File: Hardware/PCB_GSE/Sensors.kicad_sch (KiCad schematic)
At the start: 18 parts, among them J6 Screw_Terminal_01x04, J7 Screw_Terminal_01x04, U1 MAX6612MXK, U4 INA125UA/2K5

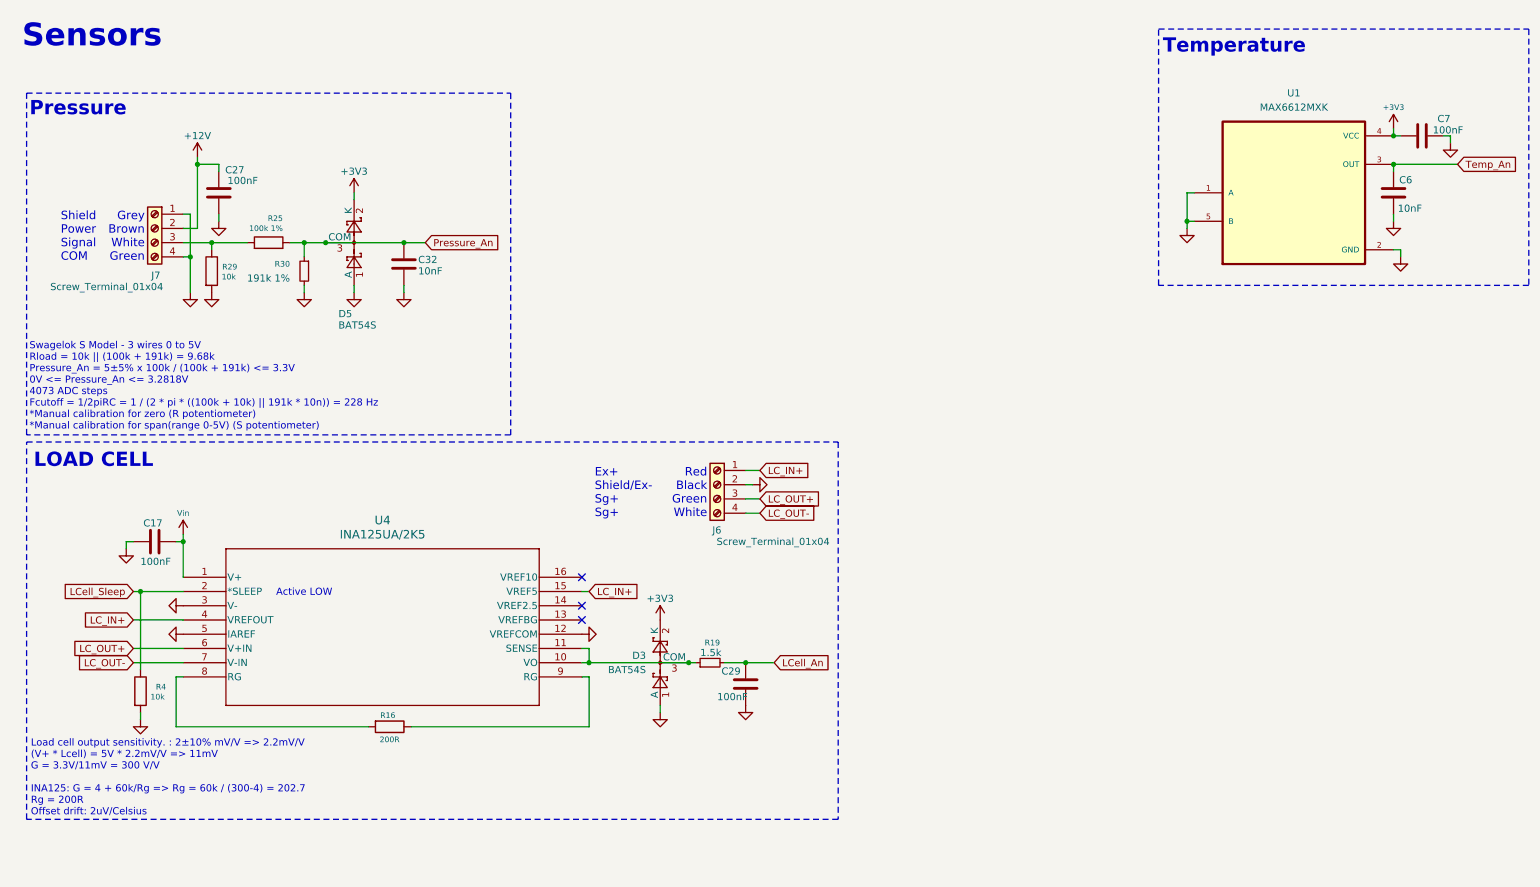
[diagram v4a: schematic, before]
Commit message: fix : BOM errors, change cutoff freq for moteur, minor fixes for GSE
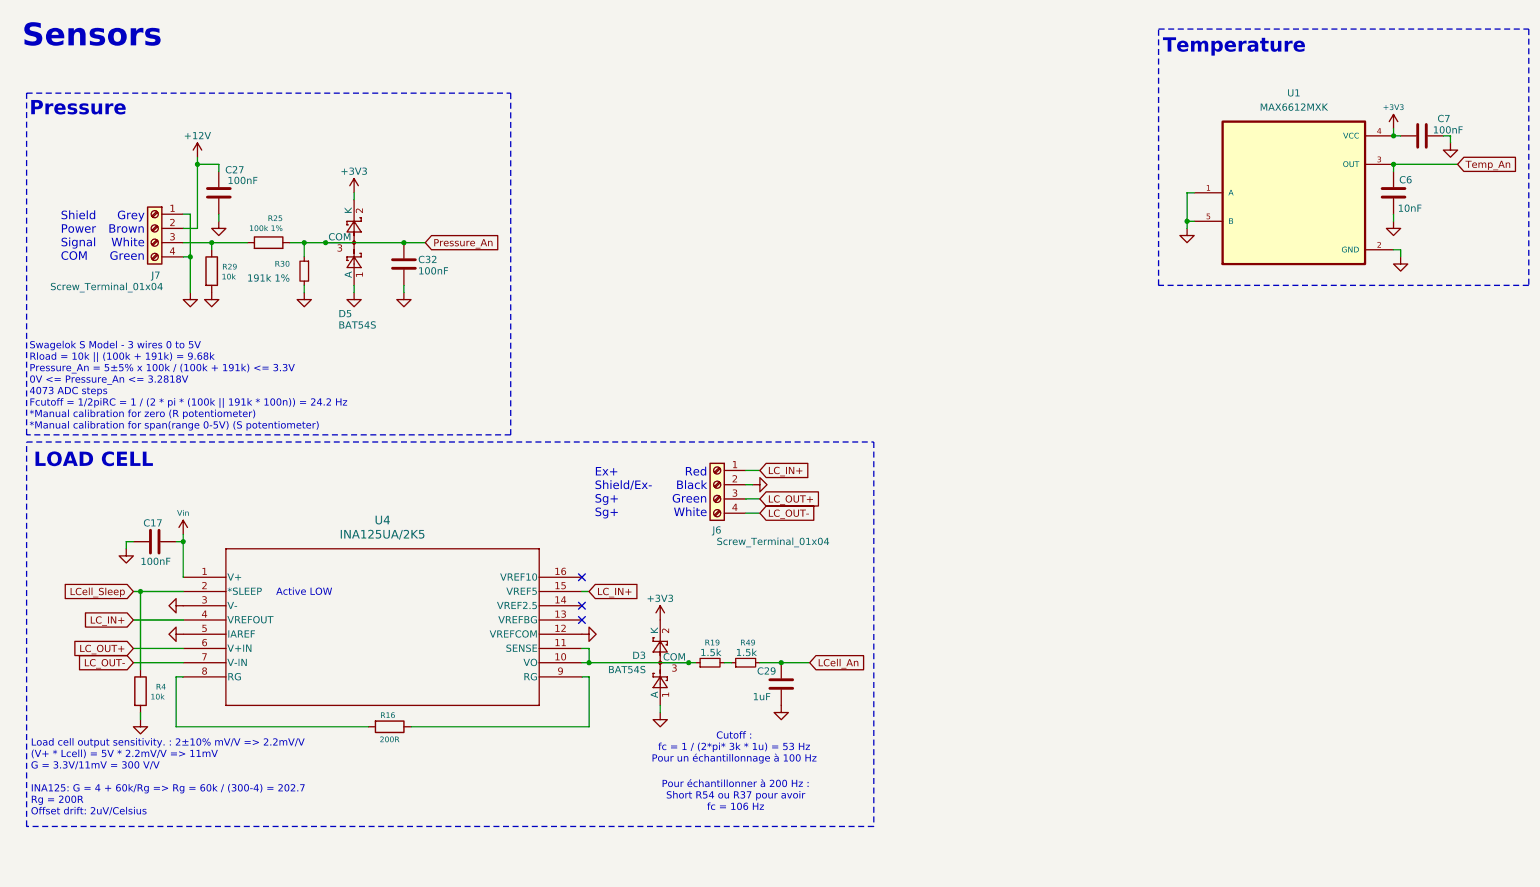
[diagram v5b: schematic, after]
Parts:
- added R49: 1.5k, Resistor_SMD:R_0805_2012Metric, symbol Device:R_Small
- C29: value 100nF -> 1uF; footprint Capacitor_SMD:C_0603_1608Metric -> Capacitor_SMD:C_0805_2012Metric; DigiKey_Part_Number 399-C0603C104K3RACTUCT-ND -> 399-C0603C105K4RACTUCT-ND; Manufacturer_Part_Number C0603C104K3RACTU -> C0603C105K4RACTU
- C32: value 10nF -> 100nF; footprint Capacitor_SMD:C_0805_2012Metric -> Capacitor_SMD:C_0603_1608Metric; DigiKey_Part_Number 1276-2434-1-ND -> 399-C0603C104K3RACTUCT-ND; Manufacturer_Part_Number CL21B103KAANNNC -> C0603C104K3RACTU
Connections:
- net LCell_An: now also R49.2; no longer R19.2
- new net: R19.2, R49.1
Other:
- note added: "Cutoff : fc = 1 / (2*pi* 3k * 1u) = 53 Hz Pour un échantillonnage à 100 Hz"
- note added: "Pour échantillonner à 200 Hz : Short R54 ou R37 pour avoir fc = 106 Hz"
- note added: "Swagelok S Model - 3 wires 0 to 5V Rload = 10k || (100k + 191k) = 9.68k Pressure_An = 5±5% x 100k / (100k + 191k) <= 3.3V 0V <= Pressure_An <= 3.2818V 4073 ADC steps Fcutoff = 1/2piRC = 1 / (2 * pi * (100k || 191k * 100n)) = 24.2 Hz *Manual calibration for zero (R potentiometer) *Manual calibration for span(range 0-5V) (S potentiometer)"
- note removed: "Swagelok S Model - 3 wires 0 to 5V Rload = 10k || (100k + 191k) = 9.68k Pressure_An = 5±5% x 100k / (100k + 191k) <= 3.3V 0V <= Pressure_An <= 3.2818V 4073 ADC steps Fcutoff = 1/2piRC = 1 / (2 * pi * ((100k + 10k) || 191k * 10n)) = 228 Hz *Manual calibration for zero (R potentiometer) *Manual calibration for span(range 0-5V) (S potentiometer)"
- moved on the sheet: C29
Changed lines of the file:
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@@
 	(rectangle
 		(start 13.97 88.9)
-		(end 158.75 156.21)
+		(end 165.1 157.48)
 		(stroke
 			(width 0)
@@
 		)
 	)
-	(text "Swagelok S Model - 3 wires 0 to 5V\nRload = 10k || (100k + 191k) = 9.68k\nPressure_An = 5±5% x 100k / (100k + 191k) <= 3.3V\n0V <= Pressure_An <= 3.2818V\n4073 ADC steps\nFcutoff = 1/2piRC = 1 / (2 * pi * ((100k + 10k) || 191k * 10n)) = 228 Hz\n*Manual calibration for zero (R potentiometer)\n*Manual calibration for span(range 0-5V) (S potentiometer)"
+	(text "Pour échantillonner à 200 Hz :\nShort R54 ou R37 pour avoir\nfc = 106 Hz"
+		(exclude_from_sim no)
+		(at 140.462 152.146 0)
+		(effects
+			(font
+				(size 1.27 1.27)
+			)
+		)
+	)
+	(text "Swagelok S Model - 3 wires 0 to 5V\nRload = 10k || (100k + 191k) = 9.68k\nPressure_An = 5±5% x 100k / (100k + 191k) <= 3.3V\n0V <= Pressure_An <= 3.2818V\n4073 ADC steps\nFcutoff = 1/2piRC = 1 / (2 * pi * (100k || 191k * 100n)) = 24.2 Hz\n*Manual calibration for zero (R potentiometer)\n*Manual calibration for span(range 0-5V) (S potentiometer)"
 		(exclude_from_sim no)
 		(at 14.478 78.994 0)
@@
 		)
 	)
+	(text "Cutoff :\nfc = 1 / (2*pi* 3k * 1u) = 53 Hz\nPour un échantillonnage à 100 Hz"
+		(exclude_from_sim no)
+		(at 140.208 143.51 0)
+		(effects
+			(font
+				(size 1.27 1.27)
+			)
+		)
+	)
 	(text "Grey\nBrown\nWhite\nGreen"
 		(exclude_from_sim no)
@@
 	)
 	(junction
+		(at 148.59 128.27)
+		(diameter 0)
+		(color 0 0 0 0)
+	)
+	(junction
 		(at 34.29 115.57)
 		(diameter 0)
@@
 		(color 0 0 0 0)
 	)
-	(junction
-		(at 142.24 128.27)
-		(diameter 0)
-		(color 0 0 0 0)
-	)
 	(no_connect
 		(at 113.03 118.11)
@@
 	(wire
 		(pts
+			(xy 148.59 128.27) (xy 153.67 128.27)
+		)
+		(stroke
+			(width 0)
+			(type default)
+		)
+	)
+	(wire
+		(pts
 			(xy 82.55 139.7) (xy 114.3 139.7)
 		)
@@
 	(wire
 		(pts
-			(xy 138.43 128.27) (xy 142.24 128.27)
-		)
-		(stroke
-			(width 0)
-			(type default)
-		)
-	)
-	(wire
-		(pts
-			(xy 142.24 128.27) (xy 147.32 128.27)
-		)
-		(stroke
-			(width 0)
-			(type default)
-		)
-	)
-	(wire
-		(pts
 			(xy 63.5 60.96) (xy 63.5 62.23)
 		)
@@
 	(wire
 		(pts
+			(xy 138.43 128.27) (xy 139.7 128.27)
+		)
+		(stroke
+			(width 0)
+			(type default)
+		)
+	)
+	(wire
+		(pts
 			(xy 41.91 113.03) (xy 41.91 106.68)
 		)
@@
 		)
 	)
+	(wire
+		(pts
+			(xy 144.78 128.27) (xy 148.59 128.27)
+		)
+		(stroke
+			(width 0)
+			(type default)
+		)
+	)
 	(global_label "LCell_An"
 		(shape input)
-		(at 147.32 128.27 0)
+		(at 153.67 128.27 0)
 		(fields_autoplaced yes)
 		(effects
@@
 		)
 		(property "Intersheetrefs" "${INTERSHEET_REFS}"
-			(at 158.2275 128.27 0)
+			(at 164.5775 128.27 0)
 			(effects
 				(font
@@
 	)
 	(symbol
+		(lib_id "Device:R_Small")
+		(at 142.24 128.27 90)
+		(unit 1)
+		(exclude_from_sim no)
+		(in_bom yes)
+		(on_board yes)
+		(dnp no)
+		(property "Reference" "R49"
+			(at 144.018 124.714 90)
+			(effects
+				(font
+					(size 1.016 1.016)
+				)
+				(justify left)
+			)
+		)
+		(property "Value" "1.5k"
+			(at 144.272 126.492 90)
+			(effects
+				(font
+					(size 1.27 1.27)
+				)
+				(justify left)
+			)
+		)
+		(property "Footprint" "Resistor_SMD:R_0805_2012Metric"
+			(at 142.24 128.27 0)
+			(effects
+				(font
+					(size 1.27 1.27)
+				)
+				(hide yes)
+			)
+		)
+		(property "Datasheet" "https://www.digikey.ca/en/products/detail/panasonic-electronic-components/ERA-3AEB152V/1465858"
+			(at 142.24 128.27 0)
+			(effects
+				(font
+					(size 1.27 1.27)
+				)
+				(hide yes)
+			)
+		)
+		(property "Description" "Resistor, small symbol"
+			(at 142.24 128.27 0)
+			(effects
+				(font
+					(size 1.27 1.27)
+				)
+				(hide yes)
+			)
+		)
+		(property "DigiKey_Part_Number" "P1.5KDBCT-ND"
+			(at 142.24 128.27 90)
+			(effects
+				(font
+					(size 1.27 1.27)
+				)
+				(hide yes)
+			)
+		)
+		(property "Manufacturer_Part_Number" "ERA-3AEB152V"
+			(at 142.24 128.27 90)
+			(effects
+				(font
+					(size 1.27 1.27)
+				)
+				(hide yes)
+			)
+		)
+		(pin "1"
+		)
+		(pin "2"
+		)
+		(instances
+			(project "PCB_GSE"
+				(path "/a63f9ed4-21e4-42d0-8bfc-f96143f84d4d/03aa44f0-76dc-422b-9f36-66afc2e68b3b"
+					(reference "R49")
+					(unit 1)
+				)
+			)
+		)
+	)
+	(symbol
 		(lib_id "Device:C")
 		(at 262.89 34.29 90)
@@
 	(symbol
 		(lib_id "Device:C")
-		(at 142.24 132.08 0)
+		(at 148.59 132.08 0)
 		(unit 1)
 		(exclude_from_sim no)
@@
 		(dnp no)
 		(property "Reference" "C29"
-			(at 137.922 129.794 0)
+			(at 144.272 129.794 0)
 			(effects
 				(font
@@
 			)
 		)
-		(property "Value" "100nF"
-			(at 137.16 134.366 0)
+		(property "Value" "1uF"
+			(at 143.51 134.366 0)
 			(effects
 				(font
@@
 			)
 		)
-		(property "Footprint" "Capacitor_SMD:C_0603_1608Metric"
-			(at 143.2052 135.89 0)
+		(property "Footprint" "Capacitor_SMD:C_0805_2012Metric"
+			(at 149.5552 135.89 0)
 			(effects
 				(font
@@
 			)
 		)
-		(property "Datasheet" "https://www.digikey.ca/en/products/detail/kemet/C0603C104K3RACTU/416044"
-			(at 142.24 132.08 0)
+		(property "Datasheet" "https://www.digikey.ca/en/products/detail/kemet/C0603C105K4RACTU/2199788"
+			(at 148.59 132.08 0)
 			(effects
 				(font
@@
 		)
 		(property "Description" "Unpolarized capacitor"
-			(at 142.24 132.08 0)
+			(at 148.59 132.08 0)
 			(effects
 				(font
@@
 			)
 		)
-		(property "DigiKey_Part_Number" "399-C0603C104K3RACTUCT-ND"
-			(at 142.24 132.08 0)
+		(property "DigiKey_Part_Number" "399-C0603C105K4RACTUCT-ND"
+			(at 148.59 132.08 0)
 			(effects
 				(font
@@
 			)
 		)
-		(property "Manufacturer_Part_Number" "C0603C104K3RACTU"
-			(at 142.24 132.08 0)
+		(property "Manufacturer_Part_Number" "C0603C105K4RACTU"
+			(at 148.59 132.08 0)
 			(effects
 				(font
@@
 			)
 		)
-		(property "Value" "10nF"
+		(property "Value" "100nF"
 			(at 83.82 58.42 0)
 			(effects
@@
 			)
 		)
-		(property "Footprint" "Capacitor_SMD:C_0805_2012Metric"
+		(property "Footprint" "Capacitor_SMD:C_0603_1608Metric"
 			(at 82.2452 60.96 0)
 			(effects
@@
 			)
 		)
-		(property "Datasheet" "https://www.digikey.ca/en/products/detail/samsung-electro-mechanics/CL21B103KAANNNC/3888092"
+		(property "Datasheet" "https://www.digikey.ca/en/products/detail/kemet/C0603C104K3RACTU/416044"
 			(at 81.28 57.15 0)
 			(effects
@@
 			)
 		)
-		(property "DigiKey_Part_Number" "1276-2434-1-ND"
+		(property "DigiKey_Part_Number" "399-C0603C104K3RACTUCT-ND"
 			(at 81.28 57.15 0)
 			(effects
@@
 			)
 		)
-		(property "Manufacturer_Part_Number" "CL21B103KAANNNC"
+		(property "Manufacturer_Part_Number" "C0603C104K3RACTU"
 			(at 81.28 57.15 0)
 			(effects
@@
 	(symbol
 		(lib_id "power:GND")
-		(at 142.24 135.89 0)
+		(at 148.59 135.89 0)
 		(unit 1)
 		(exclude_from_sim no)
@@
 		(fields_autoplaced yes)
 		(property "Reference" "#PWR0224"
-			(at 142.24 142.24 0)
+			(at 148.59 142.24 0)
 			(effects
 				(font
@@
 		)
 		(property "Value" "GND"
-			(at 142.24 140.97 0)
+			(at 148.59 140.97 0)
 			(effects
 				(font
@@
 		)
 		(property "Footprint" ""
-			(at 142.24 135.89 0)
+			(at 148.59 135.89 0)
 			(effects
 				(font
@@
 		)
 		(property "Datasheet" ""
-			(at 142.24 135.89 0)
+			(at 148.59 135.89 0)
 			(effects
 				(font
@@
 		)
 		(property "Description" ""
-			(at 142.24 135.89 0)
+			(at 148.59 135.89 0)
 			(effects
 				(font

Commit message: feature : Done v1 and send to fab
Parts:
- C29: DigiKey_Part_Number 399-C0603C105K4RACTUCT-ND -> 1276-1029-1-ND; Manufacturer_Part_Number C0603C105K4RACTU -> CL21B105KBFNNNE
- D3, D5: footprint Package_TO_SOT_SMD:SOT-23 -> Package_TO_SOT_SMD:SOT-23-3
- R19, R49: DigiKey_Part_Number P1.5KDBCT-ND -> 311-1.50KCRCT-ND; Manufacturer_Part_Number ERA-3AEB152V -> RC0805FR-071K5L
- R29, R4: DigiKey_Part_Number 311-10.0KHRCT-ND -> 541-10.0KCCT-ND; Manufacturer_Part_Number RC0603FR-0710KL -> CRCW080510K0FKEA
- R30: DigiKey_Part_Number P191KDBCT-ND -> 311-191KCRCT-ND; Manufacturer_Part_Number ERA-3AEB1913V -> RC0805FR-07191KL
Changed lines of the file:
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@@
 			)
 		)
-		(property "Footprint" "Package_TO_SOT_SMD:SOT-23"
+		(property "Footprint" "Package_TO_SOT_SMD:SOT-23-3"
 			(at 75.565 51.435 0)
 			(effects
@@
 			)
 		)
-		(property "Footprint" "Package_TO_SOT_SMD:SOT-23"
+		(property "Footprint" "Package_TO_SOT_SMD:SOT-23-3"
 			(at 123.825 126.365 0)
 			(effects
@@
 			)
 		)
-		(property "Datasheet" "https://www.digikey.ca/en/products/detail/panasonic-electronic-components/ERA-3AEB152V/1465858"
+		(property "Datasheet" "https://www.digikey.ca/en/products/detail/yageo/RC0805FR-071K5L/727496"
 			(at 135.89 128.27 0)
 			(effects
@@
 			)
 		)
-		(property "DigiKey_Part_Number" "P1.5KDBCT-ND"
+		(property "DigiKey_Part_Number" "311-1.50KCRCT-ND"
 			(at 135.89 128.27 90)
 			(effects
@@
 			)
 		)
-		(property "Manufacturer_Part_Number" "ERA-3AEB152V"
+		(property "Manufacturer_Part_Number" "RC0805FR-071K5L"
 			(at 135.89 128.27 90)
 			(effects
@@
 			)
 		)
-		(property "Datasheet" "https://www.digikey.ca/en/products/detail/panasonic-electronic-components/ERA-3AEB1913V/2026952"
+		(property "Datasheet" "https://www.digikey.ca/en/products/detail/yageo/RC0805FR-07191KL/727660"
 			(at 63.5 58.42 0)
 			(effects
@@
 			)
 		)
-		(property "DigiKey_Part_Number" "P191KDBCT-ND"
+		(property "DigiKey_Part_Number" "311-191KCRCT-ND"
 			(at 63.5 58.42 90)
 			(effects
@@
 			)
 		)
-		(property "Manufacturer_Part_Number" "ERA-3AEB1913V"
+		(property "Manufacturer_Part_Number" "RC0805FR-07191KL"
 			(at 63.5 58.42 90)
 			(effects
@@
 			)
 		)
-		(property "Datasheet" "https://www.digikey.ca/en/products/detail/panasonic-electronic-components/ERA-3AEB152V/1465858"
+		(property "Datasheet" "https://www.digikey.ca/en/products/detail/yageo/RC0805FR-071K5L/727496"
 			(at 142.24 128.27 0)
 			(effects
@@
 			)
 		)
-		(property "DigiKey_Part_Number" "P1.5KDBCT-ND"
+		(property "DigiKey_Part_Number" "311-1.50KCRCT-ND"
 			(at 142.24 128.27 90)
 			(effects
@@
 			)
 		)
-		(property "Manufacturer_Part_Number" "ERA-3AEB152V"
+		(property "Manufacturer_Part_Number" "RC0805FR-071K5L"
 			(at 142.24 128.27 90)
 			(effects
@@
 			)
 		)
-		(property "Datasheet" "https://www.digikey.ca/en/products/detail/yageo/RC0603FR-0710KL/726880"
+		(property "Datasheet" "https://www.digikey.ca/en/products/detail/vishay-dale/CRCW080510K0FKEA/1175751"
 			(at 46.99 58.42 0)
 			(effects
@@
 			)
 		)
-		(property "DigiKey_Part_Number" "311-10.0KHRCT-ND"
+		(property "DigiKey_Part_Number" "541-10.0KCCT-ND"
 			(at 46.99 58.42 0)
 			(effects
@@
 			)
 		)
-		(property "Manufacturer_Part_Number" "RC0603FR-0710KL"
+		(property "Manufacturer_Part_Number" "CRCW080510K0FKEA"
 			(at 46.99 58.42 0)
 			(effects
@@
 			)
 		)
-		(property "Datasheet" "https://www.digikey.ca/en/products/detail/kemet/C0603C105K4RACTU/2199788"
+		(property "Datasheet" "https://www.digikey.ca/en/products/detail/samsung-electro-mechanics/CL21B105KBFNNNE/3886687"
 			(at 148.59 132.08 0)
 			(effects
@@
 			)
 		)
-		(property "DigiKey_Part_Number" "399-C0603C105K4RACTUCT-ND"
+		(property "DigiKey_Part_Number" "1276-1029-1-ND"
 			(at 148.59 132.08 0)
 			(effects
@@
 			)
 		)
-		(property "Manufacturer_Part_Number" "C0603C105K4RACTU"
+		(property "Manufacturer_Part_Number" "CL21B105KBFNNNE"
 			(at 148.59 132.08 0)
 			(effects
@@
 			)
 		)
-		(property "Datasheet" "https://www.digikey.ca/en/products/detail/yageo/RC0603FR-0710KL/726880"
+		(property "Datasheet" "https://www.digikey.ca/en/products/detail/vishay-dale/CRCW080510K0FKEA/1175751"
 			(at 34.29 133.35 0)
 			(effects
@@
 			)
 		)
-		(property "DigiKey_Part_Number" "311-10.0KHRCT-ND"
+		(property "DigiKey_Part_Number" "541-10.0KCCT-ND"
 			(at 34.29 133.35 0)
 			(effects
@@
 			)
 		)
-		(property "Manufacturer_Part_Number" "RC0603FR-0710KL"
+		(property "Manufacturer_Part_Number" "CRCW080510K0FKEA"
 			(at 34.29 133.35 0)
 			(effects
